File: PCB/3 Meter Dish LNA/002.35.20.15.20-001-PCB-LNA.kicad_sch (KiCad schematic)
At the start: 10 parts, among them J1 Conn_Coaxial, J2 Conn_Coaxial, J3 Conn_Coaxial, U3 YAT-1A+, U4 L7805, U5 L7805

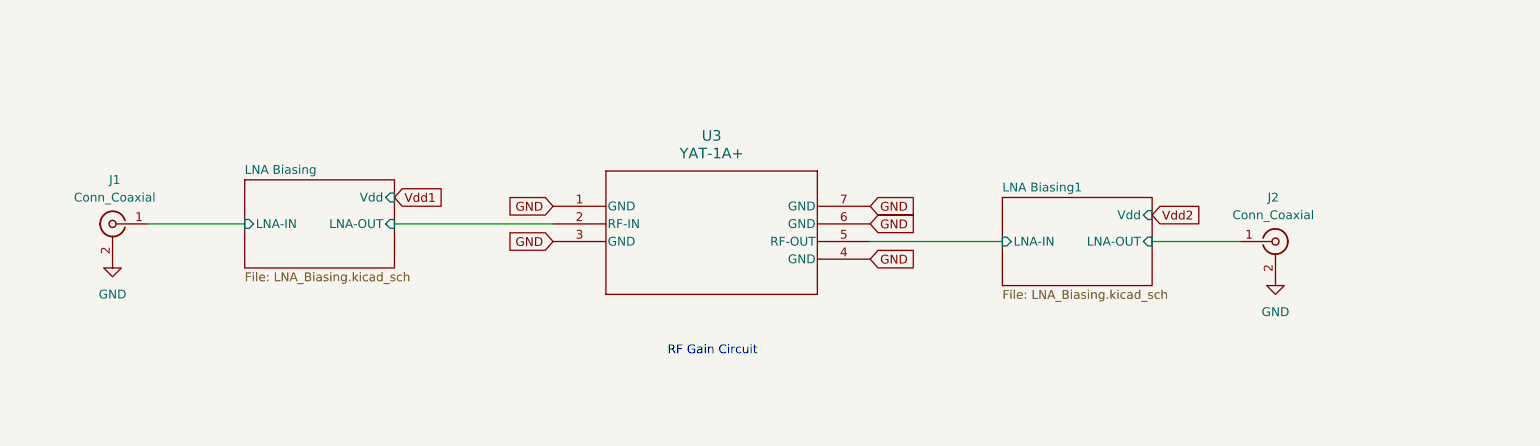
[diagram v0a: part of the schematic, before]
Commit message: Added document numbers
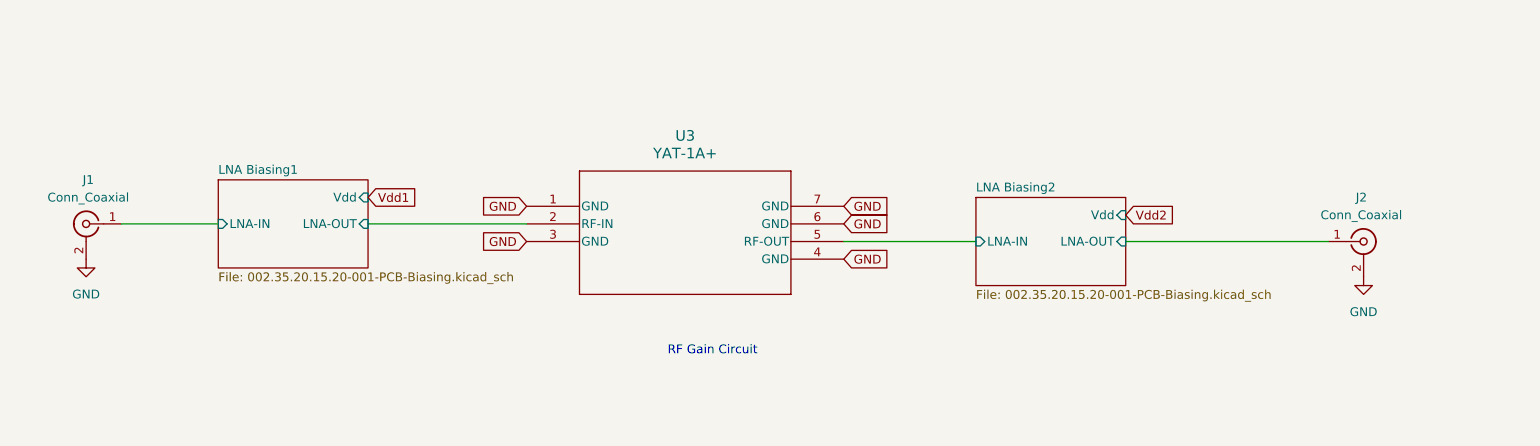
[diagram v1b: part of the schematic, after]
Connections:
- net LNA Biasing/LNA-IN is gone; now on net LNA Biasing1/LNA-IN: J1.1 (In)
- net LNA Biasing/LNA-OUT is gone; now on net LNA Biasing1/LNA-OUT: U3.2 (RF-IN)
- net LNA Biasing1/LNA-IN: no longer U3.5 (RF-OUT)
- net LNA Biasing1/LNA-OUT: no longer J2.1 (In)
- new net LNA Biasing2/LNA-IN: U3.5 (RF-OUT)
- new net LNA Biasing2/LNA-OUT: J2.1 (In)
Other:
- removed sheet LNA Biasing
- added sheet LNA Biasing2 (002.35.20.15.20-001-PCB-Biasing.kicad_sch)
- sheet LNA Biasing1: file LNA_Biasing.kicad_sch -> 002.35.20.15.20-001-PCB-Biasing.kicad_sch
- moved on the sheet: J1, J2, U3
